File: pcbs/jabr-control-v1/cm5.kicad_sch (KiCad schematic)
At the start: 1 part

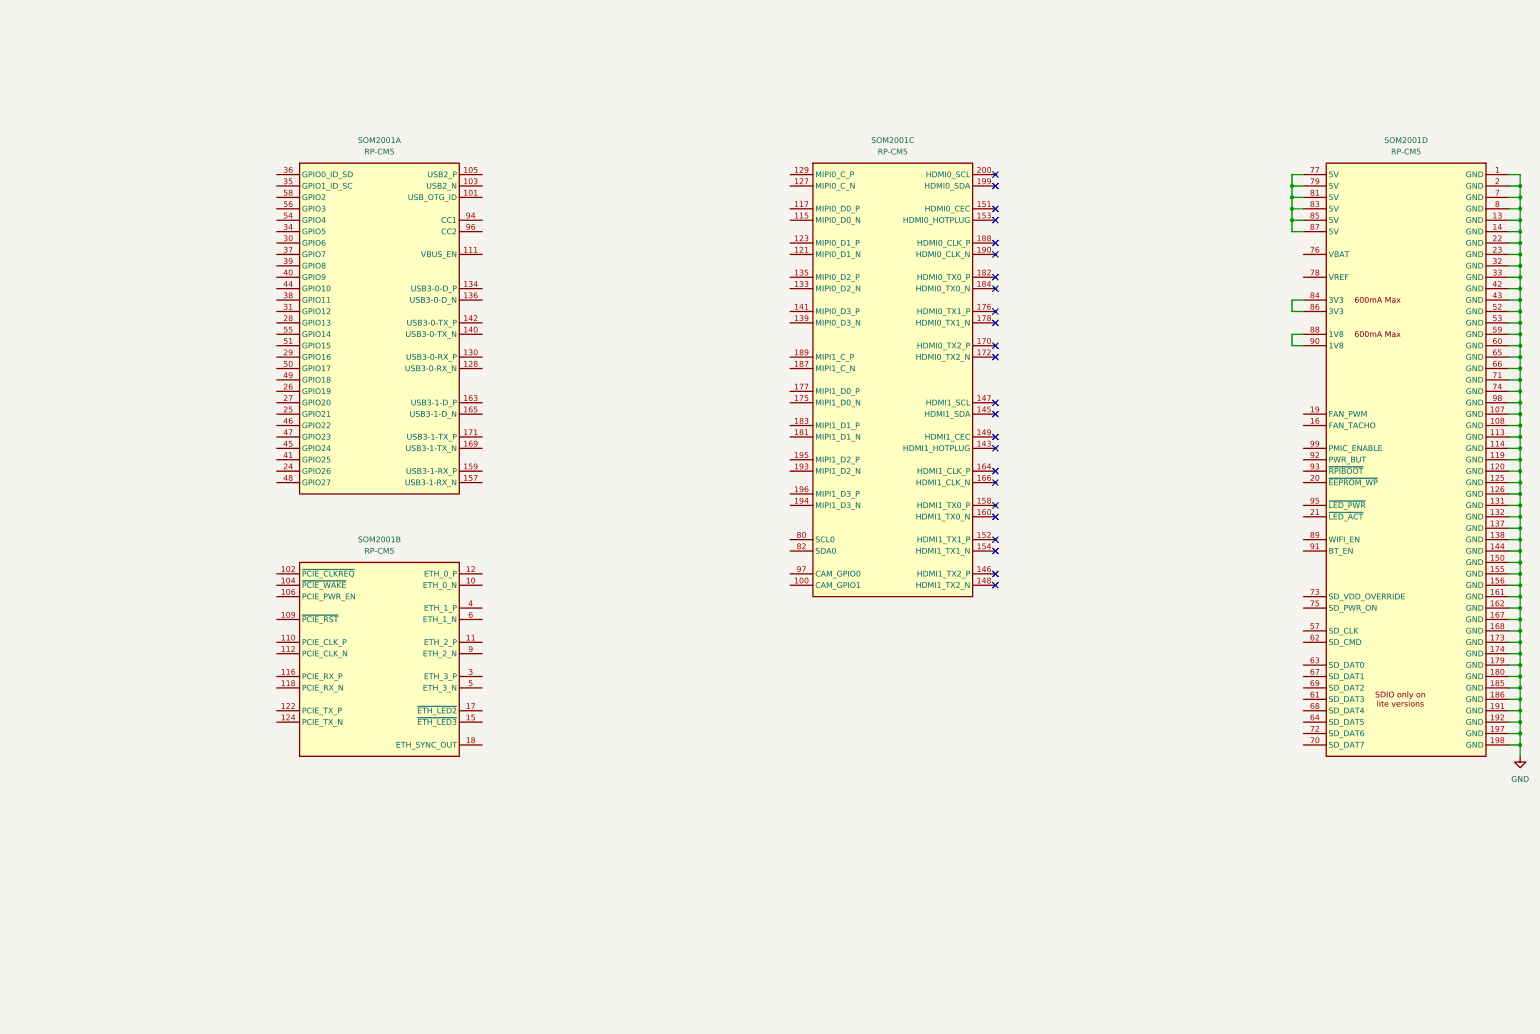
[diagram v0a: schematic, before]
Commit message: Added PCIe connections
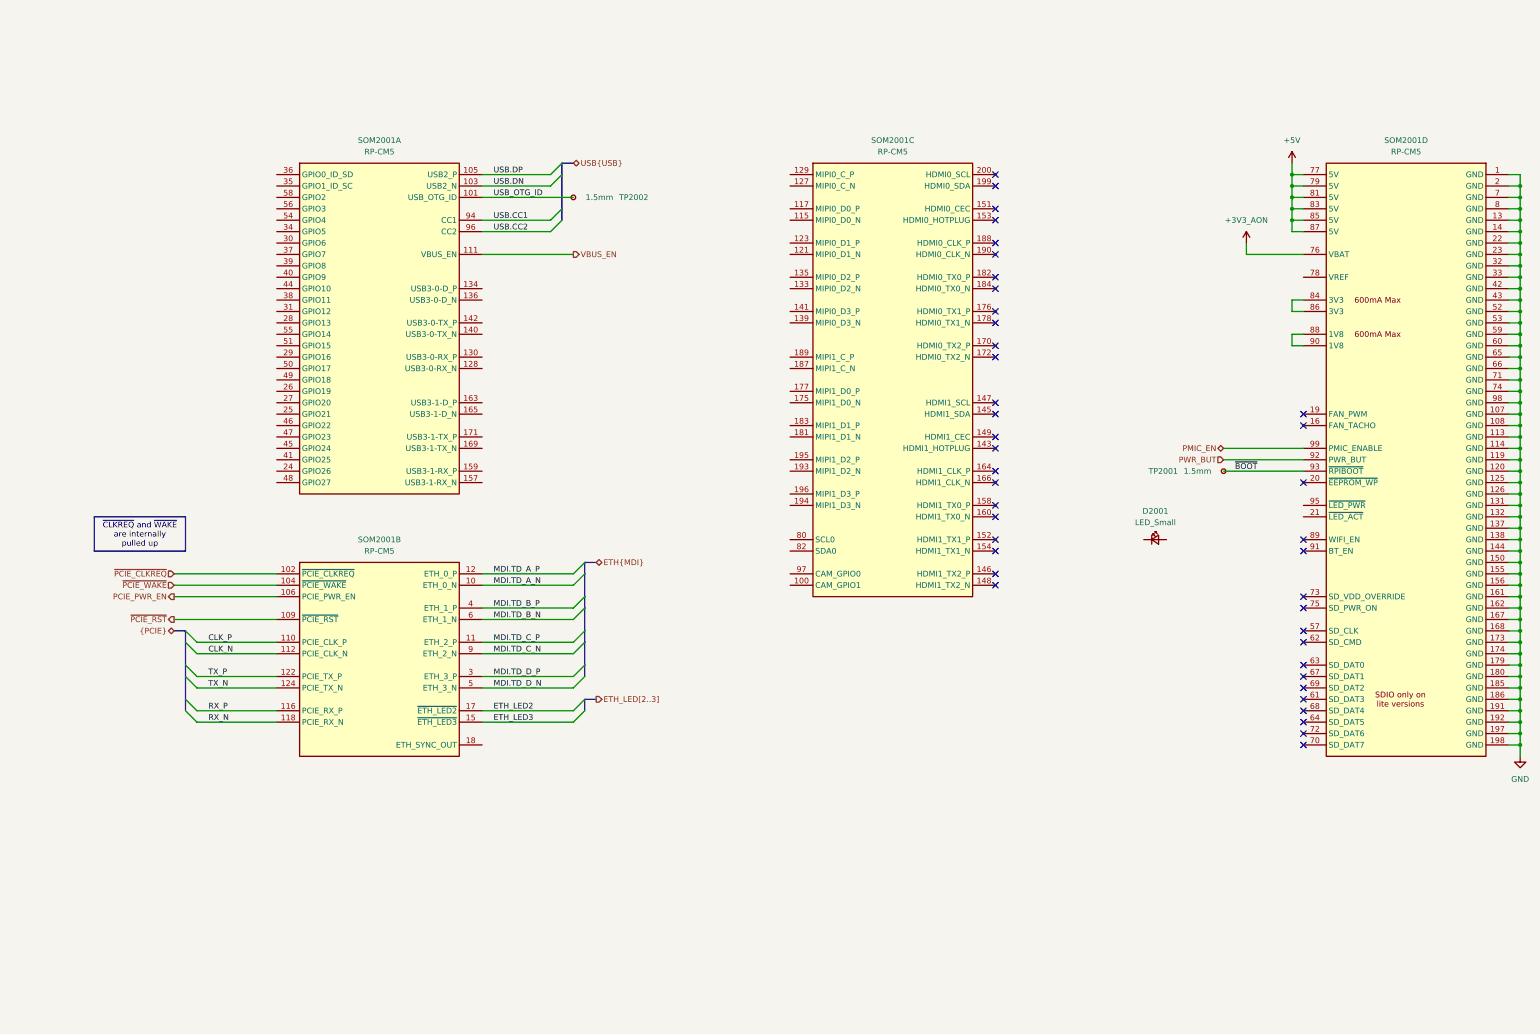
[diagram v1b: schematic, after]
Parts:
- added D2001: LED_Small, symbol Device:LED_Small
- added TP2001, TP2002: 1.5mm, TestPoint:TestPoint_Pad_D1.5mm, symbol Connector:TestPoint_Small
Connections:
- net MDI.TD_A_N: now reaches SOM2001.10 (ETH_0_N)
- net ~{PCIE_CLKREQ}: now reaches SOM2001.102 (~{PCIE_CLKREQ})
- net ~{PCIE_WAKE}: now reaches SOM2001.104 (~{PCIE_WAKE})
- net PCIE_PWR_EN: now reaches SOM2001.106 (PCIE_PWR_EN)
- net ~{PCIE_RST}: now reaches SOM2001.109 (~{PCIE_RST})
- net MDI.TD_C_P: now reaches SOM2001.11 (ETH_2_P)
- net CLK_P: now reaches SOM2001.110 (PCIE_CLK_P)
- net CLK_N: now reaches SOM2001.112 (PCIE_CLK_N)
- net RX_P: now reaches SOM2001.116 (PCIE_RX_P)
- net RX_N: now reaches SOM2001.118 (PCIE_RX_N)
- net MDI.TD_A_P: now reaches SOM2001.12 (ETH_0_P)
- net TX_P: now reaches SOM2001.122 (PCIE_TX_P)
- net TX_N: now reaches SOM2001.124 (PCIE_TX_N)
- net ETH_LED3: now reaches SOM2001.15 (~{ETH_LED3})
- net ETH_LED2: now reaches SOM2001.17 (~{ETH_LED2})
- net MDI.TD_D_P: now reaches SOM2001.3 (ETH_3_P)
- net MDI.TD_B_P: now reaches SOM2001.4 (ETH_1_P)
- net MDI.TD_D_N: now reaches SOM2001.5 (ETH_3_N)
- net MDI.TD_B_N: now reaches SOM2001.6 (ETH_1_N)
- net MDI.TD_C_N: now reaches SOM2001.9 (ETH_2_N)
- net USB_OTG_ID: now reaches SOM2001.101 (USB_OTG_ID)
- net USB_OTG_ID: now also TP2002.1
- net USB.DN: now reaches SOM2001.103 (USB2_N)
- net USB.DP: now reaches SOM2001.105 (USB2_P)
- net VBUS_EN: now reaches SOM2001.111 (VBUS_EN)
- net USB.CC1: now reaches SOM2001.94 (CC1)
- net USB.CC2: now reaches SOM2001.96 (CC2)
- net +3V3_AON: now reaches SOM2001.76 (VBAT)
- net +5V: now reaches SOM2001.77 (5V), SOM2001.79 (5V), SOM2001.81 (5V), SOM2001.83 (5V), SOM2001.85 (5V), SOM2001.87 (5V)
- net PWR_BUT: now reaches SOM2001.92 (PWR_BUT)
- net ~{BOOT}: now reaches SOM2001.93 (~{RPIBOOT})
- net ~{BOOT}: now also TP2001.1
- net PMIC_EN: now reaches SOM2001.99 (PMIC_ENABLE)
- no-connect marks 24 -> 41

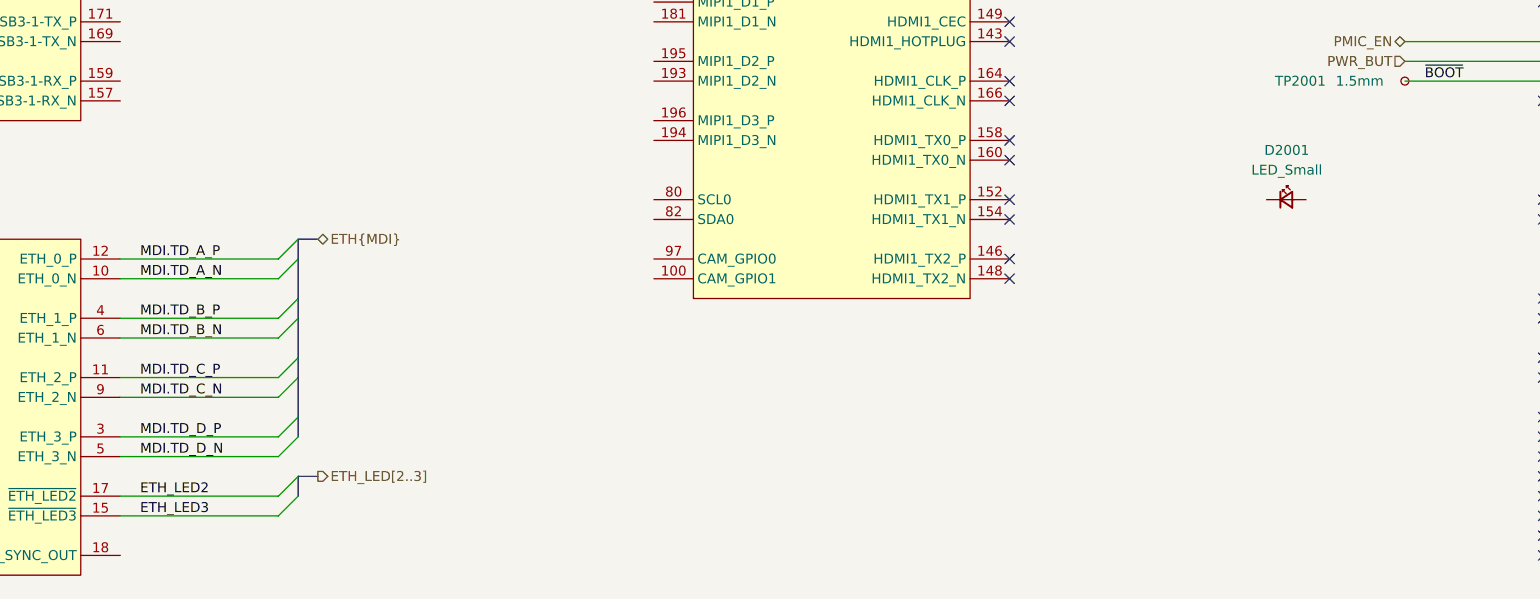
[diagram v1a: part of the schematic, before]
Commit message: Added power sheets
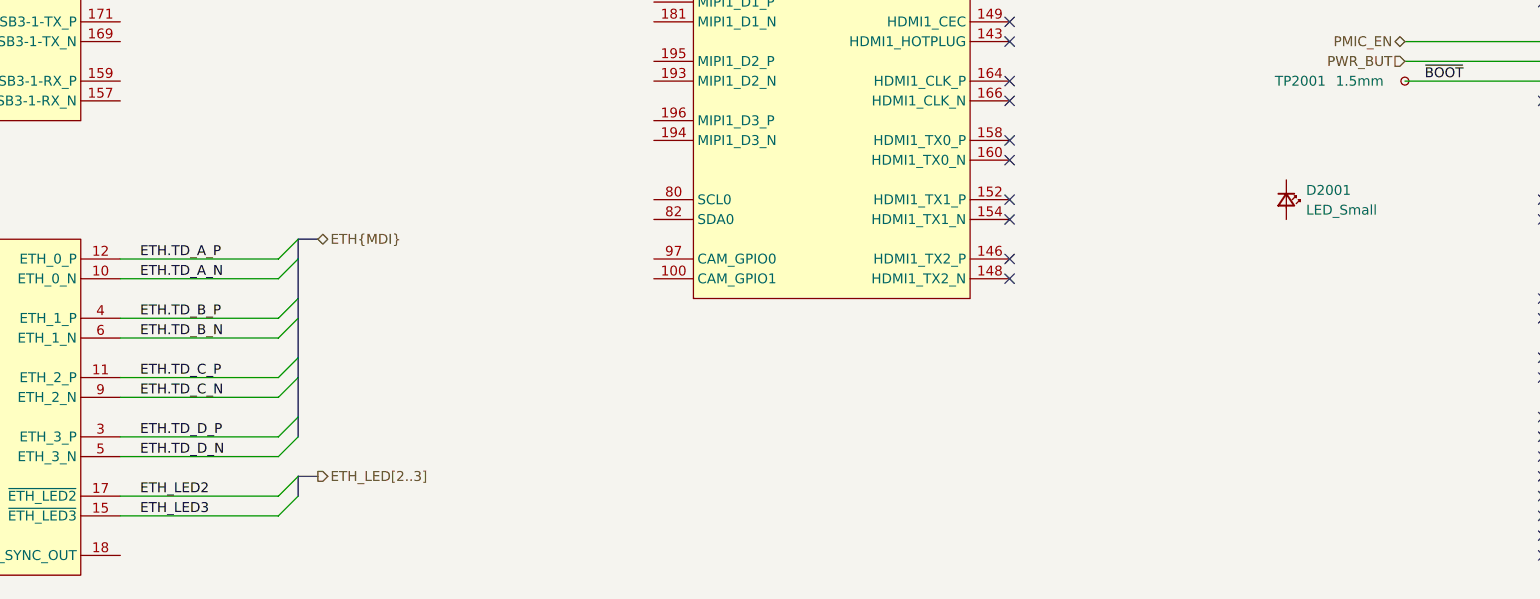
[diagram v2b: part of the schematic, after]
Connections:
- net MDI.TD_A_N renamed ETH.TD_A_N
- net MDI.TD_A_P renamed ETH.TD_A_P
- net MDI.TD_B_N renamed ETH.TD_B_N
- net MDI.TD_B_P renamed ETH.TD_B_P
- net MDI.TD_C_N renamed ETH.TD_C_N
- net MDI.TD_C_P renamed ETH.TD_C_P
- net MDI.TD_D_N renamed ETH.TD_D_N
- net MDI.TD_D_P renamed ETH.TD_D_P
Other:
- moved on the sheet: D2001
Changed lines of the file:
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@@
 		)
 	)
-	(label "MDI.TD_D_N"
-		(at 127 193.04 0)
+	(label "ETH.TD_C_P"
+		(at 127 182.88 0)
 		(effects
 			(font
@@
 		)
 	)
-	(label "MDI.TD_A_N"
+	(label "ETH.TD_A_N"
 		(at 127 170.18 0)
 		(effects
@@
 		)
 	)
-	(label "MDI.TD_D_P"
-		(at 127 190.5 0)
+	(label "ETH.TD_C_N"
+		(at 127 185.42 0)
 		(effects
 			(font
@@
 		)
 	)
+	(label "ETH.TD_D_N"
+		(at 127 193.04 0)
+		(effects
+			(font
+				(size 1.27 1.27)
+			)
+			(justify left bottom)
+		)
+	)
 	(label "~{BOOT}"
 		(at 292.1 144.78 0)
@@
 		)
 	)
+	(label "ETH.TD_A_P"
+		(at 127 167.64 0)
+		(effects
+			(font
+				(size 1.27 1.27)
+			)
+			(justify left bottom)
+		)
+	)
 	(label "CLK_N"
 		(at 63.5 185.42 0)
@@
 		)
 	)
-	(label "MDI.TD_A_P"
-		(at 127 167.64 0)
+	(label "ETH.TD_B_N"
+		(at 127 177.8 0)
+		(effects
+			(font
+				(size 1.27 1.27)
+			)
+			(justify left bottom)
+		)
+	)
+	(label "ETH.TD_B_P"
+		(at 127 175.26 0)
 		(effects
 			(font
@@
 		)
 	)
-	(label "MDI.TD_B_N"
-		(at 127 177.8 0)
-		(effects
-			(font
-				(size 1.27 1.27)
-			)
-			(justify left bottom)
-		)
-	)
-	(label "MDI.TD_C_P"
-		(at 127 182.88 0)
-		(effects
-			(font
-				(size 1.27 1.27)
-			)
-			(justify left bottom)
-		)
-	)
-	(label "MDI.TD_C_N"
-		(at 127 185.42 0)
-		(effects
-			(font
-				(size 1.27 1.27)
-			)
-			(justify left bottom)
-		)
-	)
-	(label "MDI.TD_B_P"
-		(at 127 175.26 0)
+	(label "ETH.TD_D_P"
+		(at 127 190.5 0)
 		(effects
 			(font
@@
 	(symbol
 		(lib_id "Device:LED_Small")
-		(at 274.32 160.02 0)
+		(at 274.32 160.02 270)
 		(unit 1)
 		(exclude_from_sim no)
@@
 		(fields_autoplaced yes)
 		(property "Reference" "D2001"
-			(at 274.3835 153.67 0)
-			(effects
-				(font
-					(size 1.27 1.27)
-				)
+			(at 276.86 158.8134 90)
+			(effects
+				(font
+					(size 1.27 1.27)
+				)
+				(justify left)
 			)
 		)
 		(property "Value" "LED_Small"
-			(at 274.3835 156.21 0)
-			(effects
-				(font
-					(size 1.27 1.27)
-				)
-			)
-		)
+			(at 276.86 161.3534 90)
+			(effects
+				(font
+					(size 1.27 1.27)
+				)
+				(justify left)
+			)
+		)

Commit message: Worked on power and other areas of the schematic
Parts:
- removed D2001: LED_Small, symbol Device:LED_Small
- added D202: PMEG4002EL-QYL, project_footprints:PMEG4002EL-QYL, symbol DIODE:PMEG4002EL-QYL
- added D203: RED, symbol Device:LED_Small
- added D204: GREEN, symbol Device:LED_Small
- added R201: 10k, project_footprints:R_0402, symbol DEV:R_SMALL
- added R203, R204: 1k, project_footprints:R_0402, symbol DEV:R_SMALL
- added SW201: SW_Push, symbol Switch:SW_Push
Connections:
- net GND: now also SW201.1
- net PWR_BUT: now also D202.1 (K), SW201.2
- net ~{LED_ACT}: now reaches SOM2001.21 (~{LED_ACT})
- net ~{LED_ACT}: now also D204.1 (K)
- net +3V3: now reaches SOM2001.84 (3V3), SOM2001.86 (3V3)
- net +3V3: now also R201.1, R203.1, R204.1
- net +1V8: now reaches SOM2001.88 (1V8), SOM2001.90 (1V8)
- net ~{LED_PWR}: now reaches SOM2001.95 (~{LED_PWR})
- net ~{LED_PWR}: now also D203.1 (K)
- net PMIC_EN: no longer names the net of SOM2001.99 (PMIC_ENABLE)
- new net ~{LED_PWR_A}: D204.2 (A), R203.2
- new net ~{LED_PWR_K}: D203.2 (A), R204.2
- new net ~{RST}: D202.2 (A), R201.2
- no-connect marks 41 -> 40
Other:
- moved on the sheet: TP2001

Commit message: Various small updates
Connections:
- net +3V3: now also SOM2001.78 (VREF)
- net ~{WL_DISABLE}: now reaches SOM2001.89 (WIFI_EN)
- net ~{BT_DISABLE}: now reaches SOM2001.91 (BT_EN)
- no-connect marks 40 -> 38
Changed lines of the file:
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@@
 	)
 	(junction
-		(at 294.64 106.68)
-		(diameter 0)
-		(color 0 0 0 0)
-	)
-	(junction
 		(at 355.6 180.34)
 		(diameter 0)
@@
 	)
 	(junction
-		(at 281.94 106.68)
+		(at 281.94 101.6)
 		(diameter 0)
 		(color 0 0 0 0)
@@
 	)
 	(junction
+		(at 294.64 101.6)
+		(diameter 0)
+		(color 0 0 0 0)
+	)
+	(junction
 		(at 355.6 157.48)
 		(diameter 0)
@@
 	)
 	(junction
+		(at 304.8 101.6)
+		(diameter 0)
+		(color 0 0 0 0)
+	)
+	(junction
 		(at 355.6 172.72)
 		(diameter 0)
@@
 	)
 	(no_connect
-		(at 307.34 165.1)
-	)
-	(no_connect
 		(at 238.76 137.16)
 	)
@@
 	)
 	(no_connect
-		(at 307.34 162.56)
-	)
-	(no_connect
 		(at 307.34 203.2)
 	)
@@
 	(wire
 		(pts
-			(xy 281.94 106.68) (xy 294.64 106.68)
+			(xy 281.94 101.6) (xy 294.64 101.6)
 		)
 		(stroke
@@
 	(wire
 		(pts
+			(xy 304.8 101.6) (xy 304.8 106.68)
+		)
+		(stroke
+			(width 0)
+			(type default)
+		)
+	)
+	(wire
+		(pts
 			(xy 355.6 200.66) (xy 355.6 203.2)
 		)
@@
 	(wire
 		(pts
+			(xy 307.34 101.6) (xy 304.8 101.6)
+		)
+		(stroke
+			(width 0)
+			(type default)
+		)
+	)
+	(wire
+		(pts
 			(xy 289.56 154.94) (xy 307.34 154.94)
 		)
@@
 	(wire
 		(pts
+			(xy 281.94 101.6) (xy 281.94 119.38)
+		)
+		(stroke
+			(width 0)
+			(type default)
+		)
+	)
+	(wire
+		(pts
 			(xy 355.6 162.56) (xy 355.6 165.1)
 		)
@@
 	(wire
 		(pts
-			(xy 294.64 106.68) (xy 294.64 119.38)
-		)
-		(stroke
-			(width 0)
-			(type default)
-		)
-	)
-	(wire
-		(pts
 			(xy 124.46 88.9) (xy 139.7 88.9)
 		)
@@
 	(wire
 		(pts
-			(xy 281.94 106.68) (xy 281.94 119.38)
-		)
-		(stroke
-			(width 0)
-			(type default)
-		)
-	)
-	(wire
-		(pts
 			(xy 307.34 96.52) (xy 294.64 96.52)
 		)
@@
 	(wire
 		(pts
-			(xy 294.64 106.68) (xy 304.8 106.68)
+			(xy 294.64 101.6) (xy 304.8 101.6)
 		)
 		(stroke
@@
 	(wire
 		(pts
-			(xy 281.94 104.14) (xy 281.94 106.68)
+			(xy 281.94 99.06) (xy 281.94 101.6)
 		)
 		(stroke
@@
 	(wire
 		(pts
+			(xy 304.8 165.1) (xy 307.34 165.1)
+		)
+		(stroke
+			(width 0)
+			(type default)
+		)
+	)
+	(wire
+		(pts
 			(xy 355.6 104.14) (xy 355.6 106.68)
 		)
@@
 	(wire
 		(pts
+			(xy 304.8 162.56) (xy 307.34 162.56)
+		)
+		(stroke
+			(width 0)
+			(type default)
+		)
+	)
+	(wire
+		(pts
 			(xy 355.6 144.78) (xy 353.06 144.78)
 		)
@@
 	(wire
 		(pts
+			(xy 294.64 101.6) (xy 294.64 119.38)
+		)
+		(stroke
+			(width 0)
+			(type default)
+		)
+	)
+	(wire
+		(pts
 			(xy 355.6 185.42) (xy 355.6 187.96)
 		)
@@
 		)
 	)
+	(hierarchical_label "I2C2{I2C}"
+		(shape bidirectional)
+		(at 241.3 213.36 180)
+		(effects
+			(font
+				(size 1.27 1.27)
+			)
+			(justify right)
+		)
+	)
 	(hierarchical_label "ETH_LED[2..3]"
 		(shape output)
@@
 		)
 	)
+	(hierarchical_label "~{BT_DISABLE}"
+		(shape output)
+		(at 304.8 165.1 180)
+		(effects
+			(font
+				(size 1.27 1.27)
+			)
+			(justify right)
+		)
+	)
 	(hierarchical_label "{PCIE}"
 		(shape bidirectional)
@@
 		)
 	)
+	(hierarchical_label "~{WL_DISABLE}"
+		(shape output)
+		(at 304.8 162.56 180)
+		(effects
+			(font
+				(size 1.27 1.27)
+			)
+			(justify right)
+		)
+	)
 	(hierarchical_label "PCIE_PWR_EN"
 		(shape output)
@@
 	(symbol
 		(lib_id "power:+3V3")
-		(at 281.94 104.14 0)
+		(at 281.94 99.06 0)
 		(unit 1)
 		(exclude_from_sim no)
@@
 		(fields_autoplaced yes)
 		(property "Reference" "#PWR0203"
-			(at 281.94 107.95 0)
+			(at 281.94 102.87 0)
 			(effects
 				(font
@@
 		)
 		(property "Value" "+3V3"
-			(at 281.94 99.06 0)
+			(at 281.94 93.98 0)
 			(effects
 				(font
@@
 		)
 		(property "Footprint" ""
-			(at 281.94 104.14 0)
+			(at 281.94 99.06 0)
 			(effects
 				(font
@@
 		)
 		(property "Datasheet" ""
-			(at 281.94 104.14 0)
+			(at 281.94 99.06 0)
 			(effects
 				(font
@@
 		)
 		(property "Description" "Power symbol creates a global label with name \"+3V3\""
-			(at 281.94 104.14 0)
+			(at 281.94 99.06 0)
 			(effects
 				(font

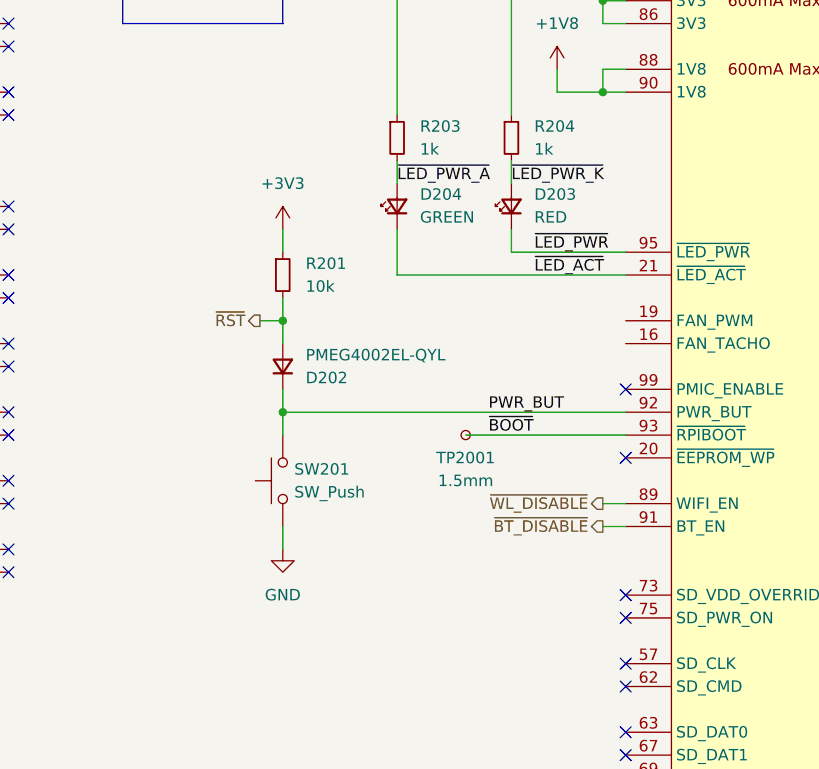
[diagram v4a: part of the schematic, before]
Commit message: Progress on LAN7431 power
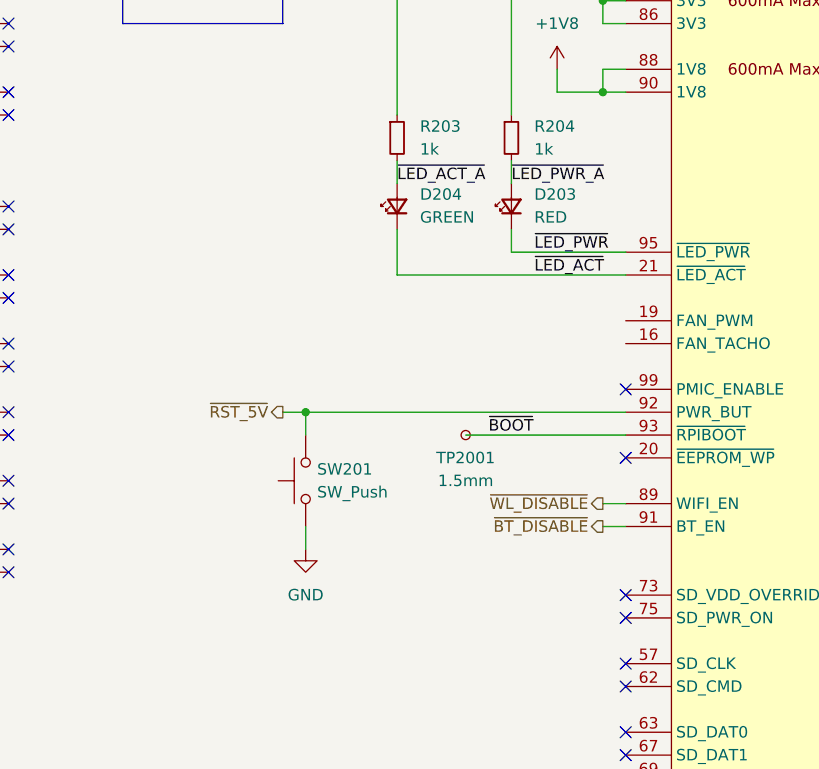
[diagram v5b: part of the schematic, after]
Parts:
- removed D202: PMEG4002EL-QYL, project_footprints:PMEG4002EL-QYL, symbol DIODE:PMEG4002EL-QYL
- removed R201: 10k, project_footprints:R_0402, symbol DEV:R_SMALL
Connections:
- net ~{LED_PWR_K} is gone; now on net ~{LED_PWR_A}: D203.2 (A), R204.2
- net ~{LED_PWR_A}: no longer D204.2 (A), R203.2
- net PWR_BUT renamed ~{RST_5V}
- new net ~{LED_ACT_A}: D204.2 (A), R203.2
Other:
- moved on the sheet: SW201
